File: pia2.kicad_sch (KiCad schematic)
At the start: 34 parts, among them IC4 74ACT02, IC8 LM393DR, IC9 CD4050BDR, J2 6-bit DAC, U11 W65C21

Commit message: Progress routing
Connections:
- net A0: now also U11.39 (RS0)
- net A1: now also U11.38 (RS1)
- net D0: now also U11.36 (D0)
- net D1: now also U11.35 (D1)
- net D2: now also U11.34 (D2)
- net D3: now also U11.33 (D3)
- net D4: now also U11.32 (D4)
- net D5: now also U11.31 (D5)
- net D6: now also U11.30 (D6)
- net D7: now also U11.29 (D7)
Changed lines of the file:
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@@
 	)
 	(bus_entry
-		(at 44.45 52.07)
+		(at 44.831 52.07)
 		(size 2.54 -2.54)
 		(stroke
@@
 	)
 	(bus_entry
-		(at 44.45 39.37)
+		(at 44.831 39.37)
 		(size 2.54 -2.54)
 		(stroke
@@
 	)
 	(bus_entry
-		(at 44.45 46.99)
+		(at 44.831 46.99)
 		(size 2.54 -2.54)
 		(stroke
@@
 	)
 	(bus_entry
-		(at 44.45 41.91)
+		(at 44.831 41.91)
 		(size 2.54 -2.54)
 		(stroke
@@
 	)
 	(bus_entry
-		(at 44.45 49.53)
+		(at 44.831 49.53)
 		(size 2.54 -2.54)
 		(stroke
@@
 	)
 	(bus_entry
-		(at 44.45 57.15)
+		(at 44.831 57.15)
 		(size 2.54 -2.54)
 		(stroke
@@
 	)
 	(bus_entry
-		(at 44.45 54.61)
+		(at 44.831 54.61)
 		(size 2.54 -2.54)
 		(stroke
@@
 	)
 	(bus_entry
-		(at 44.45 44.45)
+		(at 44.831 44.45)
 		(size 2.54 -2.54)
 		(stroke
@@
 	(wire
 		(pts
-			(xy 46.99 52.07) (xy 49.53 52.07)
+			(xy 47.371 52.07) (xy 49.911 52.07)
 		)
 		(stroke
@@
 	(bus
 		(pts
-			(xy 44.45 46.99) (xy 44.45 44.45)
+			(xy 44.831 46.99) (xy 44.831 44.45)
 		)
 		(stroke
@@
 	(wire
 		(pts
-			(xy 46.99 49.53) (xy 49.53 49.53)
-		)
-		(stroke
-			(width 0)
-			(type default)
-		)
-	)
-	(wire
-		(pts
-			(xy 45.72 73.66) (xy 49.53 73.66)
+			(xy 47.371 49.53) (xy 49.911 49.53)
+		)
+		(stroke
+			(width 0)
+			(type default)
+		)
+	)
+	(wire
+		(pts
+			(xy 45.72 73.66) (xy 49.911 73.66)
 		)
 		(stroke
@@
 	(bus
 		(pts
-			(xy 44.45 41.91) (xy 44.45 39.37)
-		)
-		(stroke
-			(width 0)
-			(type default)
-		)
-	)
-	(wire
-		(pts
-			(xy 46.99 46.99) (xy 49.53 46.99)
+			(xy 44.831 41.91) (xy 44.831 39.37)
+		)
+		(stroke
+			(width 0)
+			(type default)
+		)
+	)
+	(wire
+		(pts
+			(xy 47.371 46.99) (xy 49.911 46.99)
 		)
 		(stroke
@@
 	(bus
 		(pts
-			(xy 44.45 54.61) (xy 44.45 52.07)
+			(xy 44.831 54.61) (xy 44.831 52.07)
 		)
 		(stroke
@@
 	(wire
 		(pts
-			(xy 46.99 54.61) (xy 49.53 54.61)
-		)
-		(stroke
-			(width 0)
-			(type default)
-		)
-	)
-	(wire
-		(pts
-			(xy 46.99 39.37) (xy 49.53 39.37)
+			(xy 47.371 54.61) (xy 49.911 54.61)
+		)
+		(stroke
+			(width 0)
+			(type default)
+		)
+	)
+	(wire
+		(pts
+			(xy 47.371 39.37) (xy 49.911 39.37)
 		)
 		(stroke
@@
 	(bus
 		(pts
-			(xy 44.45 44.45) (xy 44.45 41.91)
+			(xy 44.831 44.45) (xy 44.831 41.91)
 		)
 		(stroke
@@
 	(wire
 		(pts
-			(xy 46.99 36.83) (xy 49.53 36.83)
+			(xy 47.371 36.83) (xy 49.911 36.83)
 		)
 		(stroke
@@
 	(bus
 		(pts
-			(xy 44.45 49.53) (xy 44.45 52.07)
+			(xy 44.831 49.53) (xy 44.831 52.07)
 		)
 		(stroke
@@
 	(bus
 		(pts
-			(xy 44.45 49.53) (xy 44.45 46.99)
+			(xy 44.831 49.53) (xy 44.831 46.99)
 		)
 		(stroke
@@
 	(wire
 		(pts
-			(xy 46.99 44.45) (xy 49.53 44.45)
+			(xy 47.371 44.45) (xy 49.911 44.45)
 		)
 		(stroke
@@
 	(bus
 		(pts
-			(xy 44.45 54.61) (xy 44.45 57.15)
+			(xy 44.831 54.61) (xy 44.831 57.15)
 		)
 		(stroke
@@
 	(bus
 		(pts
-			(xy 44.45 36.83) (xy 44.45 39.37)
+			(xy 44.831 36.83) (xy 44.831 39.37)
 		)
 		(stroke
@@
 	(wire
 		(pts
-			(xy 46.99 41.91) (xy 49.53 41.91)
-		)
-		(stroke
-			(width 0)
-			(type default)
-		)
-	)
-	(wire
-		(pts
-			(xy 45.72 71.12) (xy 49.53 71.12)
+			(xy 47.371 41.91) (xy 49.911 41.91)
+		)
+		(stroke
+			(width 0)
+			(type default)
+		)
+	)
+	(wire
+		(pts
+			(xy 45.72 71.12) (xy 49.911 71.12)
 		)
 		(stroke
@@
 	)
 	(label "D1"
-		(at 46.99 39.37 0)
+		(at 47.371 39.37 0)
 		(fields_autoplaced yes)
 		(effects
@@
 	)
 	(label "D7"
-		(at 46.99 54.61 0)
+		(at 47.371 54.61 0)
 		(fields_autoplaced yes)
 		(effects
@@
 	)
 	(label "D3"
-		(at 46.99 44.45 0)
+		(at 47.371 44.45 0)
 		(fields_autoplaced yes)
 		(effects
@@
 	)
 	(label "D5"
-		(at 46.99 49.53 0)
+		(at 47.371 49.53 0)
 		(fields_autoplaced yes)
 		(effects
@@
 	)
 	(label "D2"
-		(at 46.99 41.91 0)
+		(at 47.371 41.91 0)
 		(fields_autoplaced yes)
 		(effects
@@
 	)
 	(label "D4"
-		(at 46.99 46.99 0)
+		(at 47.371 46.99 0)
 		(fields_autoplaced yes)
 		(effects
@@
 	)
 	(label "D6"
-		(at 46.99 52.07 0)
+		(at 47.371 52.07 0)
 		(fields_autoplaced yes)
 		(effects
@@
 	)
 	(label "D0"
-		(at 46.99 36.83 0)
+		(at 47.371 36.83 0)
 		(fields_autoplaced yes)
 		(effects
@@
 	(hierarchical_label "D[0..7]"
 		(shape bidirectional)
-		(at 44.45 36.83 180)
-		(fields_autoplaced yes)
-		(effects
+		(at 44.831 36.83 180)
+		(fields_autoplaced yes)
+		(effects

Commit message: rework to flex atx size
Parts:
- PL5: footprint Dragon:DIN-5_DELTRON_671-0501_45deg_Horizontal -> CoCoDragonMultiPak:KMDGX-5S-N
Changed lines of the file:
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@@
 			)
 		)
-		(property "Footprint" "Dragon:DIN-5_DELTRON_671-0501_45deg_Horizontal"
+		(property "Footprint" "CoCoDragonMultiPak:KMDGX-5S-N"
 			(at 207.645 82.931 0)
 			(effects

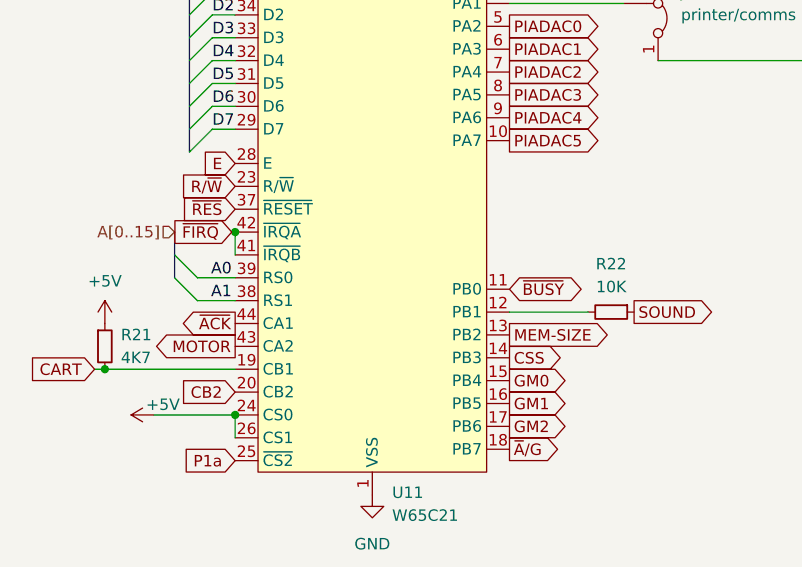
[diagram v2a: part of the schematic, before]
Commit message: migrate to flash rom
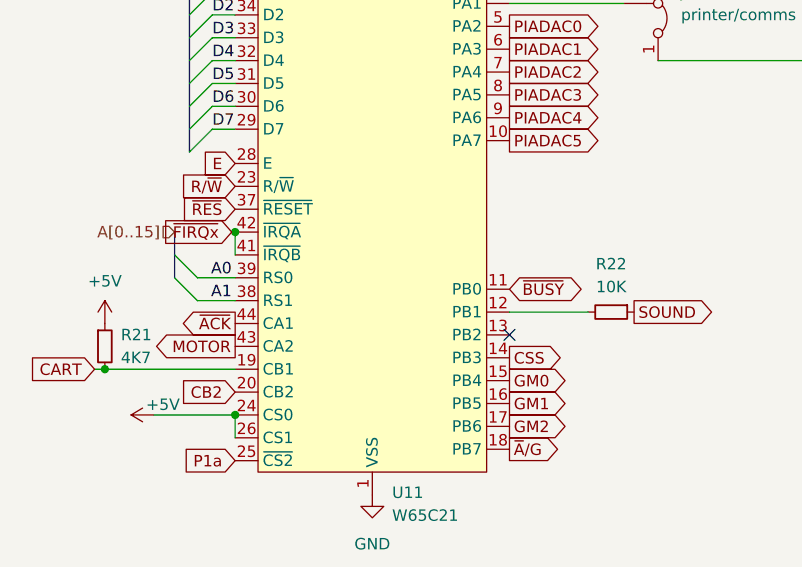
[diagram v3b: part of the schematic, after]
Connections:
- net MEM-SIZE: no longer names the net of U11.13 (PB2)
- net ~{FIRQ} renamed ~{FIRQx}
- no-connect marks 1 -> 2
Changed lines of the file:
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@@
+	)
+	(junction
+		(at 49.911 66.04)
+		(diameter 0)
+		(color 0 0 0 0)
 	)
 	(junction
@@
 	)
 	(junction
-		(at 49.911 66.04)
-		(diameter 0)
-		(color 0 0 0 0)
-	)
-	(junction
 		(at 171.704 44.958)
 		(diameter 0)
@@
 	)
 	(no_connect
+		(at 80.391 77.47)
+	)
+	(no_connect
 		(at 231.394 47.5983)
 	)
@@
 		)
 	)
-	(global_label "MEM-SIZE"
-		(shape output)
-		(at 80.391 77.47 0)
-		(fields_autoplaced yes)
-		(effects
-			(font
-				(size 1.27 1.27)
-			)
-			(justify left)
-		)
-		(property "Intersheetrefs" "${INTERSHEET_REFS}"
-			(at 92.4396 77.47 0)
-			(effects
-				(font
-					(size 1.27 1.27)
-				)
-				(justify left)
-				(hide yes)
-			)
-		)
-	)
 	(global_label "6bit D{slash}A"
 		(shape output)
@@
 		)
 	)
-	(global_label "~{FIRQ}"
-		(shape input)
-		(at 49.53 66.04 180)
-		(fields_autoplaced yes)
-		(effects
-			(font
-				(size 1.27 1.27)
-			)
-			(justify right)
-		)
-		(property "Intersheetrefs" "${INTERSHEET_REFS}"
-			(at 42.912 65.9606 0)
-			(effects
-				(font
-					(size 1.27 1.27)
-				)
-				(justify right)
-				(hide yes)
-			)
-		)
-	)
 	(global_label "MOTOR2"
 		(shape passive)
@@
 			(effects
 				(font
+					(size 1.27 1.27)
+				)
+				(justify right)
+				(hide yes)
+			)
+		)
+	)
+	(global_label "~{FIRQx}"
+		(shape input)
+		(at 49.53 66.04 180)
+		(fields_autoplaced yes)
+		(effects
+			(font
+				(size 1.27 1.27)
+			)
+			(justify right)
+		)
+		(property "Intersheetrefs" "${INTERSHEET_REFS}"
+			(at 41.2228 66.04 0)
+			(effects
+				(font

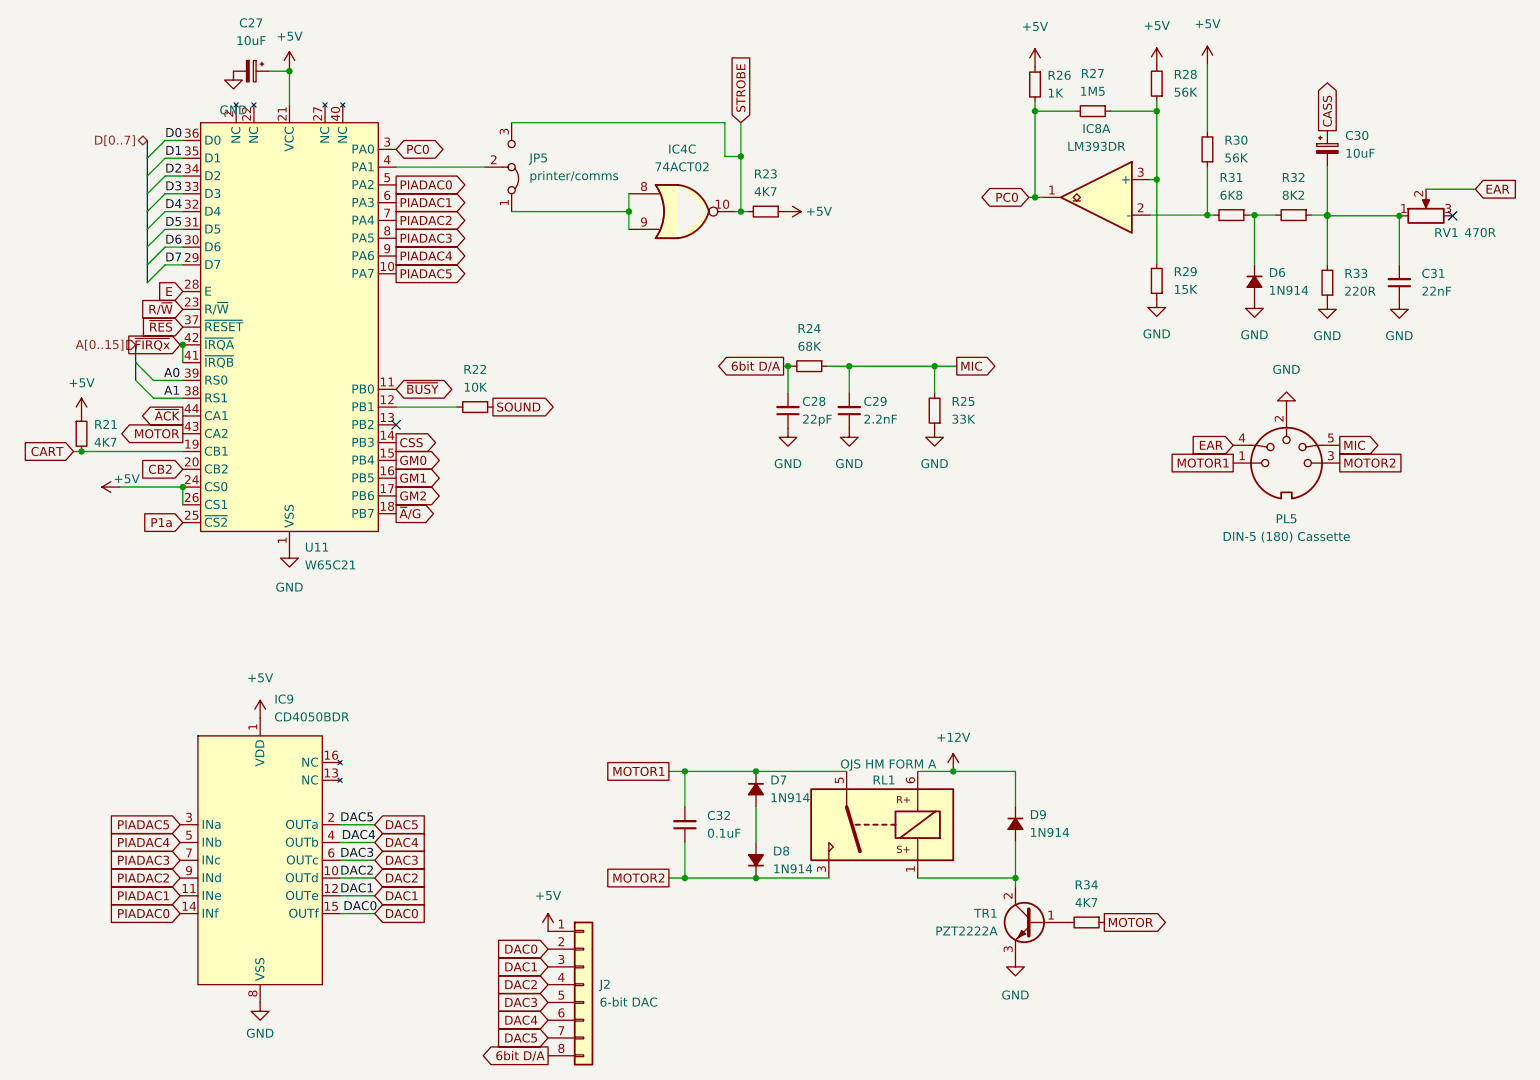
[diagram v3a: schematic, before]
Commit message: complete routing
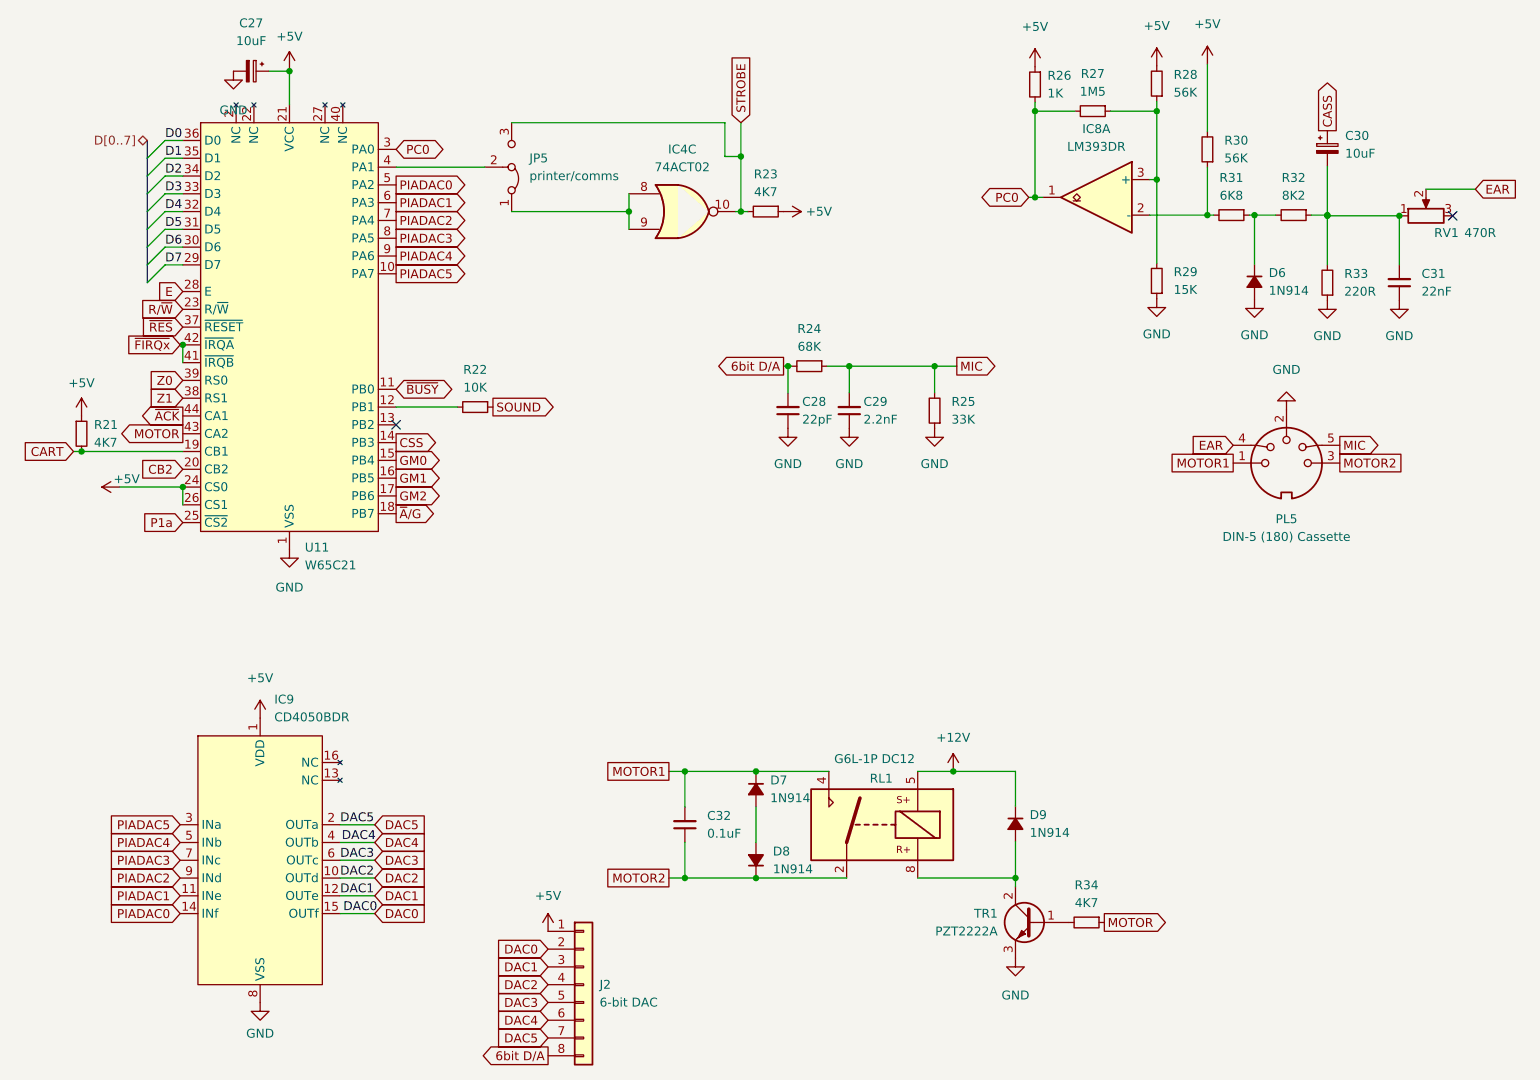
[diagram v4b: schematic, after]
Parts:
- removed RL1: OJS HM FORM A, Dragon:OJS HM 10A Relay, symbol Relay:ADW11
- added RL1: G6L-1P DC12, Dragon:Omron G6L, symbol Motorola PIA:Relay-G6L-1
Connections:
- net +12V: now also RL1.5
- net MOTOR1: now also RL1.4
- net MOTOR2: now also RL1.2
- net at D9.2 (A), TR1.2 (C): now also RL1.8
- net A0 renamed Z0
- net A1 renamed Z1
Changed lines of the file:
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@@
 	)
 	(bus_entry
-		(at 43.18 68.58)
-		(size 2.54 2.54)
-		(stroke
-			(width 0)
-			(type default)
-		)
-	)
-	(bus_entry
 		(at 44.831 39.37)
 		(size 2.54 -2.54)
@@
 	)
 	(bus_entry
-		(at 43.18 71.12)
-		(size 2.54 2.54)
-		(stroke
-			(width 0)
-			(type default)
-		)
-	)
-	(bus_entry
 		(at 44.831 46.99)
 		(size 2.54 -2.54)
@@
 	(wire
 		(pts
-			(xy 131.826 142.24) (xy 142.24 142.24)
+			(xy 131.826 142.24) (xy 144.78 142.24)
 		)
 		(stroke
@@
 	(wire
 		(pts
-			(xy 45.72 73.66) (xy 49.911 73.66)
-		)
-		(stroke
-			(width 0)
-			(type default)
-		)
-	)
-	(wire
-		(pts
 			(xy 62.23 26.924) (xy 65.151 26.924)
 		)
@@
 		)
 	)
-	(bus
-		(pts
-			(xy 43.18 71.12) (xy 43.18 68.58)
-		)
-		(stroke
-			(width 0)
-			(type default)
-		)
-	)
 	(wire
 		(pts
@@
 	(wire
 		(pts
-			(xy 131.826 127) (xy 144.78 127)
+			(xy 131.826 127) (xy 142.24 127)
 		)
 		(stroke
@@
 	(wire
 		(pts
-			(xy 45.72 71.12) (xy 49.911 71.12)
-		)
-		(stroke
-			(width 0)
-			(type default)
-		)
-	)
-	(wire
-		(pts
 			(xy 154.94 142.24) (xy 168.91 142.24)
 		)
@@
 		)
 	)
-	(bus
-		(pts
-			(xy 43.18 66.04) (xy 43.18 68.58)
-		)
-		(stroke
-			(width 0)
-			(type default)
-		)
-	)
 	(wire
 		(pts
@@
 		)
 	)
-	(label "A0"
-		(at 49.53 71.12 180)
-		(fields_autoplaced yes)
-		(effects
-			(font
-				(size 1.27 1.27)
-			)
-			(justify right bottom)
-		)
-	)
 	(label "DAC0"
 		(at 72.8456 147.32 0)
@@
 		)
 	)
-	(label "A1"
-		(at 49.53 73.66 180)
-		(fields_autoplaced yes)
-		(effects
-			(font
-				(size 1.27 1.27)
-			)
-			(justify right bottom)
-		)
-	)
 	(label "D3"
 		(at 47.371 44.45 0)
@@
 		)
 	)
+	(global_label "Z1"
+		(shape input)
+		(at 49.911 73.66 180)
+		(fields_autoplaced yes)
+		(effects
+			(font
+				(size 1.27 1.27)
+			)
+			(justify right)
+		)
+		(property "Intersheetrefs" "${INTERSHEET_REFS}"
+			(at 45.161 73.66 0)
+			(effects
+				(font
+					(size 1.27 1.27)
+				)
+				(justify right)
+				(hide yes)
+			)
+		)
+	)
 	(global_label "~{A}{slash}G"
 		(shape output)
@@
 		)
 	)
+	(global_label "Z0"
+		(shape input)
+		(at 49.911 71.12 180)
+		(fields_autoplaced yes)
+		(effects
+			(font
+				(size 1.27 1.27)
+			)
+			(justify right)
+		)
+		(property "Intersheetrefs" "${INTERSHEET_REFS}"
+			(at 45.161 71.12 0)
+			(effects
+				(font
+					(size 1.27 1.27)
+				)
+				(justify right)
+				(hide yes)
+			)
+		)
+	)
 	(global_label "PIADAC0"
 		(shape output)
@@
 		)
 	)
-	(hierarchical_label "A[0..15]"
-		(shape input)
-		(at 43.18 66.04 180)
-		(fields_autoplaced yes)
-		(effects
-			(font
-				(size 1.27 1.27)
-			)
-			(justify right)
-		)
-	)
 	(hierarchical_label "D[0..7]"
 		(shape bidirectional)
@@
 	)
 	(symbol
+		(lib_id "Motorola PIA:Relay-G6L-1")
+		(at 149.86 134.62 0)
+		(mirror y)
+		(unit 1)
+		(exclude_from_sim no)
+		(in_bom yes)
+		(on_board yes)
+		(dnp no)
+		(property "Reference" "RL1"
+			(at 148.082 128.016 0)
+			(effects
+				(font
+					(size 1.27 1.27)
+				)
+				(justify right)
+			)
+		)
+		(property "Value" "G6L-1P DC12"
+			(at 143.002 125.222 0)
+			(effects
+				(font
+					(size 1.27 1.27)
+				)
+				(justify right)
+			)
+		)
+		(property "Footprint" "Dragon:Omron G6L"
+			(at 149.86 134.62 0)
+			(effects
+				(font
+					(size 1.27 1.27)
+				)
+				(hide yes)
+			)
+		)
+		(property "Datasheet" "https://mm.digikey.com/Volume0/opasdata/d220001/medias/docus/932/G6L.pdf"
+			(at 149.86 134.62 0)
+			(effects
+				(font
+					(size 1.27 1.27)
+				)
+				(hide yes)
+			)
+		)
+		(property "Description" ""
+			(at 149.86 134.62 0)
+			(effects
+				(font
+					(size 1.27 1.27)
+				)
+				(hide yes)
+			)
+		)
+		(property "DigiKey" "Z1229-ND"
+			(at 149.86 134.62 0)
+			(effects
+				(font
+					(size 1.27 1.27)
+				)
+				(hide yes)
+			)
+		)
+		(pin "4"
+		)
+		(pin "8"
+		)
+		(pin "5"
+		)
+		(pin "2"
+		)
+		(instances
+			(project "DragonRevX4Plus"
+				(path "/280624a6-9139-42c2-8c41-e9b53b8715d2/82858fae-fa47-4af0-9ba3-6944f9c45ebd"
+					(reference "RL1")
+					(unit 1)
+				)
+			)
+		)
+	)
+	(symbol
 		(lib_id "power:GND")
 		(at 157.353 77.978 0)
@@
 					(unit 1)
 				)
-			)
-		)
-	)
-	(symbol
-		(lib_id "Relay:ADW11")
-		(at 149.86 134.62 180)
-		(unit 1)
-		(exclude_from_sim no)
-		(in_bom yes)
-		(on_board yes)
-		(dnp no)
-		(property "Reference" "RL1"
-			(at 151.765 128.27 0)
-			(effects
-				(font
-					(size 1.27 1.27)
-				)
-				(justify left)
-			)
-		)
-		(property "Value" "OJS HM FORM A"
-			(at 157.607 125.984 0)
-			(effects
-				(font
-					(size 1.27 1.27)
-				)
-				(justify left)
-			)
-		)
-		(property "Footprint" "Dragon:OJS HM 10A Relay"
-			(at 116.205 133.35 0)
-			(effects
-				(font
-					(size 1.27 1.27)
-				)
-				(hide yes)
-			)
-		)
-		(property "Datasheet" "https://www.te.com/commerce/DocumentDelivery/DDEController?Action=srchrtrv&DocNm=OJS_10A&DocType=DS&DocLang=English"
-			(at 149.86 134.62 0)
-			(effects
-				(font
-					(size 1.27 1.27)
-				)
-				(hide yes)
-			)
-		)
-		(property "Description" ""
-			(at 149.86 134.62 0)
-			(effects
-				(font
-					(size 1.27 1.27)
-				)
-				(hide yes)
-			)
-		)
-		(property "DigiKey" "41-OJS-SH-105HMF,00000-ND"
-			(at 149.86 134.62 0)
-			(effects
-				(font
-					(size 1.27 1.27)
-				)
-				(hide yes)
-			)
-		)
-		(pin "1"
-		)
-		(pin "3"
-		)
-		(pin "5"
-		)
-		(pin "6"
-		)
-		(instances
-			(project "DragonRevX4Plus"
-				(path "/280624a6-9139-42c2-8c41-e9b53b8715d2/82858fae-fa47-4af0-9ba3-6944f9c45ebd"
-					(reference "RL1")
-					(unit 1)
-				)
